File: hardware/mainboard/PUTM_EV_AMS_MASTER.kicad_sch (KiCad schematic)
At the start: 21 parts, among them J1 Conn_02x10_Odd_Even, J10 M300-MV10345M1, J3 Conn_02x04_Odd_Even, J4 FTSH-107-01-L-D-K, J5 M80-51004XX, J7 M300-MV10345M1, J8 M80-51004XX, T1 SM91502ALE

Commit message: First board revision
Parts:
- added H1: MountingHole_Pad, MountingHole:MountingHole_3.2mm_M3_Pad_Via, symbol Mechanical:MountingHole_Pad
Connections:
- net GND: now also H1.1
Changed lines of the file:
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@@
 	(wire
 		(pts
-			(xy 182.88 231.14) (xy 158.75 231.14)
+			(xy 158.75 231.14) (xy 184.15 231.14)
 		)
 		(stroke
@@
 	(wire
 		(pts
-			(xy 182.88 266.7) (xy 151.13 266.7)
+			(xy 151.13 266.7) (xy 184.15 266.7)
+		)
+		(stroke
+			(width 0)
+			(type default)
+		)
+	)
+	(wire
+		(pts
+			(xy 323.85 222.25) (xy 323.85 223.52)
 		)
 		(stroke
@@
 	(wire
 		(pts
-			(xy 182.88 264.16) (xy 153.67 264.16)
+			(xy 153.67 264.16) (xy 184.15 264.16)
 		)
 		(stroke
@@
 	(wire
 		(pts
-			(xy 182.88 261.62) (xy 156.21 261.62)
+			(xy 156.21 261.62) (xy 184.15 261.62)
 		)
 		(stroke
@@
 		(lib_name "GND_5")
 		(lib_id "power:GND")
+		(at 323.85 223.52 0)
+		(unit 1)
+		(exclude_from_sim no)
+		(in_bom yes)
+		(on_board yes)
+		(dnp no)
+		(property "Reference" "#PWR04"
+			(at 323.85 229.87 0)
+			(effects
+				(font
+					(size 1.27 1.27)
+				)
+				(hide yes)
+			)
+		)
+		(property "Value" "GND"
+			(at 323.85 227.33 0)
+			(effects
+				(font
+					(size 1.27 1.27)
+				)
+			)
+		)
+		(property "Footprint" ""
+			(at 323.85 223.52 0)
+			(effects
+				(font
+					(size 1.27 1.27)
+				)
+				(hide yes)
+			)
+		)
+		(property "Datasheet" ""
+			(at 323.85 223.52 0)
+			(effects
+				(font
+					(size 1.27 1.27)
+				)
+				(hide yes)
+			)
+		)
+		(property "Description" ""
+			(at 323.85 223.52 0)
+			(effects
+				(font
+					(size 1.27 1.27)
+				)
+				(hide yes)
+			)
+		)
+		(pin "1"
+		)
+		(instances
+			(project "PUTM_EV_AMS_MASTER"
+				(path "/b456cffc-d9d7-4c91-91f2-36ec9a65dd1b"
+					(reference "#PWR04")
+					(unit 1)
+				)
+			)
+		)
+	)
+	(symbol
+		(lib_name "GND_5")
+		(lib_id "power:GND")
 		(at 364.49 223.52 0)
 		(unit 1)
@@
 					(unit 1)
 				)
+			)
+		)
+	)
+	(symbol
+		(lib_id "Mechanical:MountingHole_Pad")
+		(at 323.85 219.71 0)
+		(unit 1)
+		(exclude_from_sim no)
+		(in_bom no)
+		(on_board yes)
+		(dnp no)
+		(fields_autoplaced yes)
+		(property "Reference" "H1"
+			(at 326.39 217.1699 0)
+			(effects
+				(font
+					(size 1.27 1.27)
+				)
+				(justify left)
+			)
+		)
+		(property "Value" "MountingHole_Pad"
+			(at 326.39 219.7099 0)
+			(effects
+				(font
+					(size 1.27 1.27)
+				)
+				(justify left)
+			)
+		)
+		(property "Footprint" "MountingHole:MountingHole_3.2mm_M3_Pad_Via"
+			(at 323.85 219.71 0)
+			(effects
+				(font
+					(size 1.27 1.27)
+				)
+				(hide yes)
+			)
+		)
+		(property "Datasheet" "~"
+			(at 323.85 219.71 0)
+			(effects
+				(font
+					(size 1.27 1.27)
+				)
+				(hide yes)
+			)
+		)
+		(property "Description" "Mounting Hole with connection"
+			(at 323.85 219.71 0)
+			(effects
+				(font
+					(size 1.27 1.27)
+				)
+				(hide yes)
+			)
+		)
+		(pin "1"
+		)
+		(instances
+			(project ""
+				(path "/b456cffc-d9d7-4c91-91f2-36ec9a65dd1b"
+					(reference "H1")
+					(unit 1)
+				)

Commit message: Layout again
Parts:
- removed H1: MountingHole_Pad, MountingHole:MountingHole_3.2mm_M3_Pad_Via, symbol Mechanical:MountingHole_Pad
- added D24, D28: 3.6V/400W, Package_TO_SOT_SMD:SOT-23-6, symbol Power_Protection:ESDA5V3SC5
- added TP19, TP20, TP21, TP22, TP23, TP24, TP25, TP26, TP27, TP28, TP29, TP30, TP31, TP32, TP33, TP34, TP35, TP36, TP37, TP38, TP39, TP40, TP41, TP42, TP43, TP44, TP45: TestPoint_Small, TestPoint:TestPoint_Pad_D1.0mm, symbol Connector:TestPoint_Small
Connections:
- net ADC/ACU_V+: now also TP38.1
- net ADC/ACU_V-: now also TP37.1
- net ADC/CAR_V+: now also TP39.1
- net ADC/CAR_V-: now also TP40.1
- net AED: now also TP26.1
- net AIR_M-: now also D28.4 (A)
- net AIR_P-: now also D28.3 (A)
- net AIR_PRE-: now also D28.1 (A)
- net AMD: now also TP27.1
- net APD: now also TP28.1
- net CAR_I: now also TP36.1
- net CRX1: now also TP22.1
- net CRX2: now also TP20.1
- net CTSMS: now also TP30.1
- net CTX1: now also TP21.1
- net CTX2: now also TP19.1
- net Connectivity/UART_RST: now also TP23.1
- net DCH: now also TP29.1
- net FAN1-: now also D24.6 (A)
- net FAN2-: now also D24.4 (A)
- net FAN3-: now also D24.3 (A)
- net FAN4-: now also D24.1 (A)
- net GND: now also D24.2 (K), D24.5 (NC), D28.2 (K), D28.5 (NC)
- net Isolated SPI/OUT+: now also TP41.1
- net Isolated SPI/OUT-: now also TP42.1
- net NRST: now also TP33.1
- net SWCLK: now also TP34.1
- net SWDIO: now also TP35.1
- net UART_DBG_RX: now also TP31.1
- net UART_DBG_TX: now also TP32.1
- net UCRX: now also TP44.1
- net UCTX: now also TP43.1
- net URX: now also TP24.1
- net UTX: now also TP25.1
- net ~{FLT}: now also TP45.1
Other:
- moved on the sheet: J3

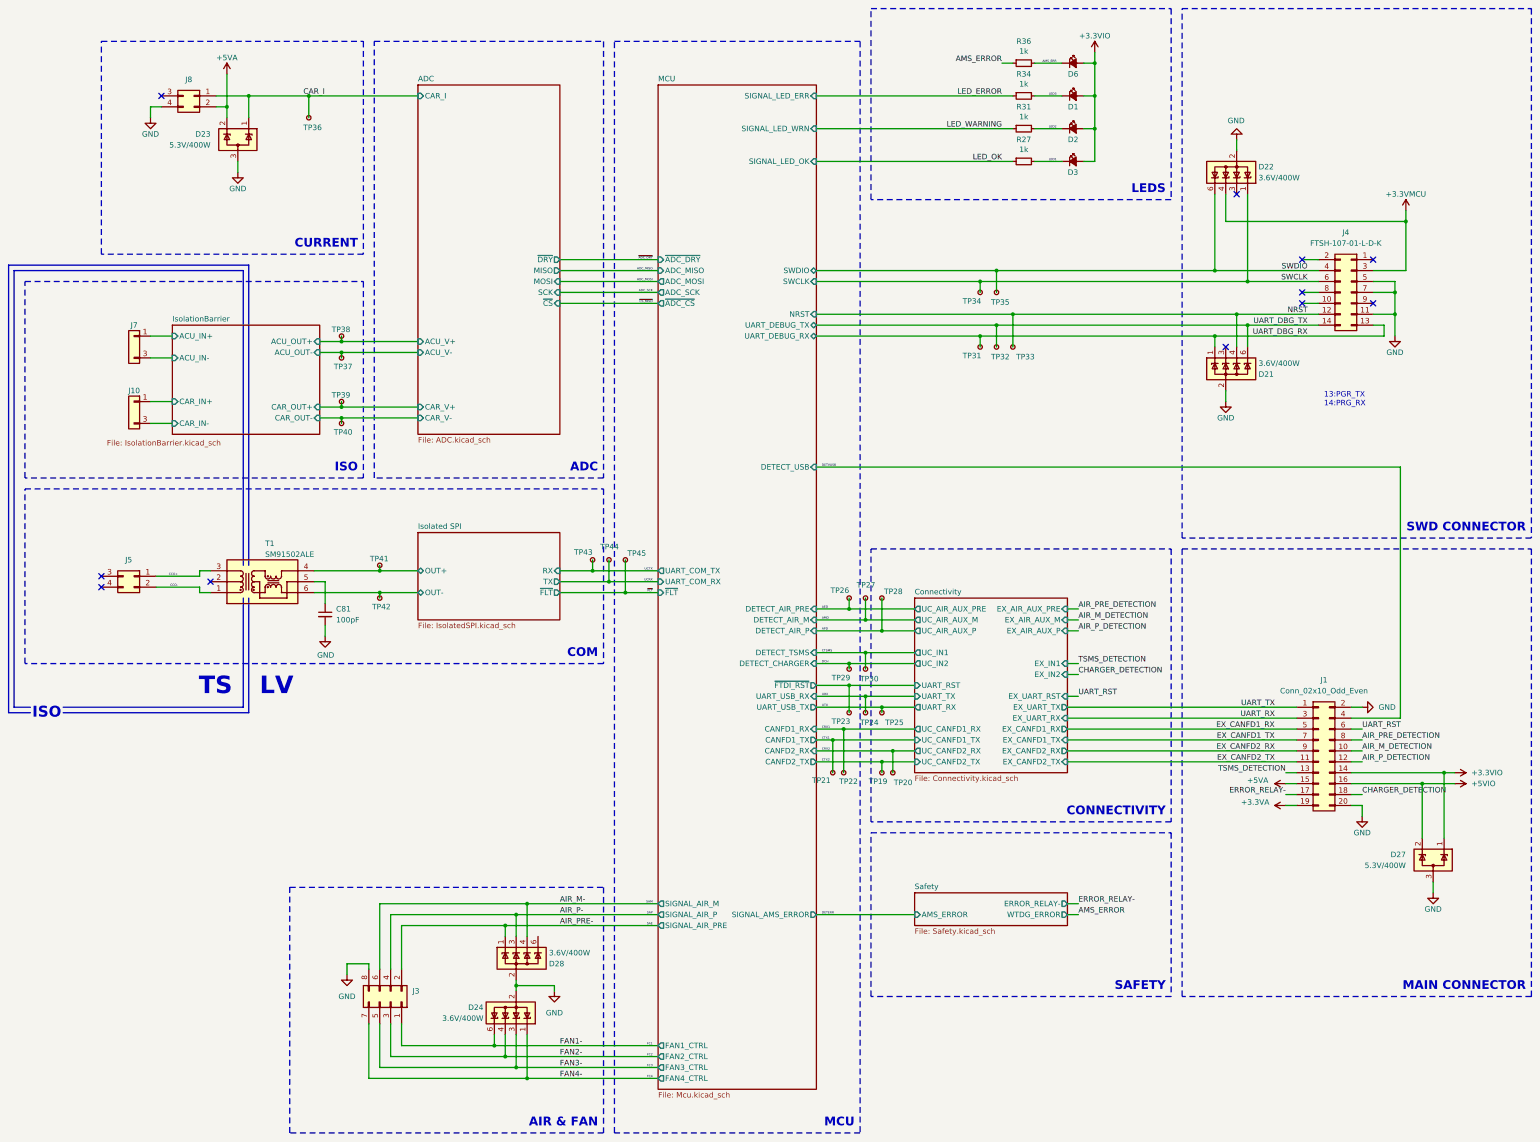
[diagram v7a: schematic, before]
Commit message: Plytka chyba fajnie zrobiona oprocz teardropow bo kicad 10 jest dziwny
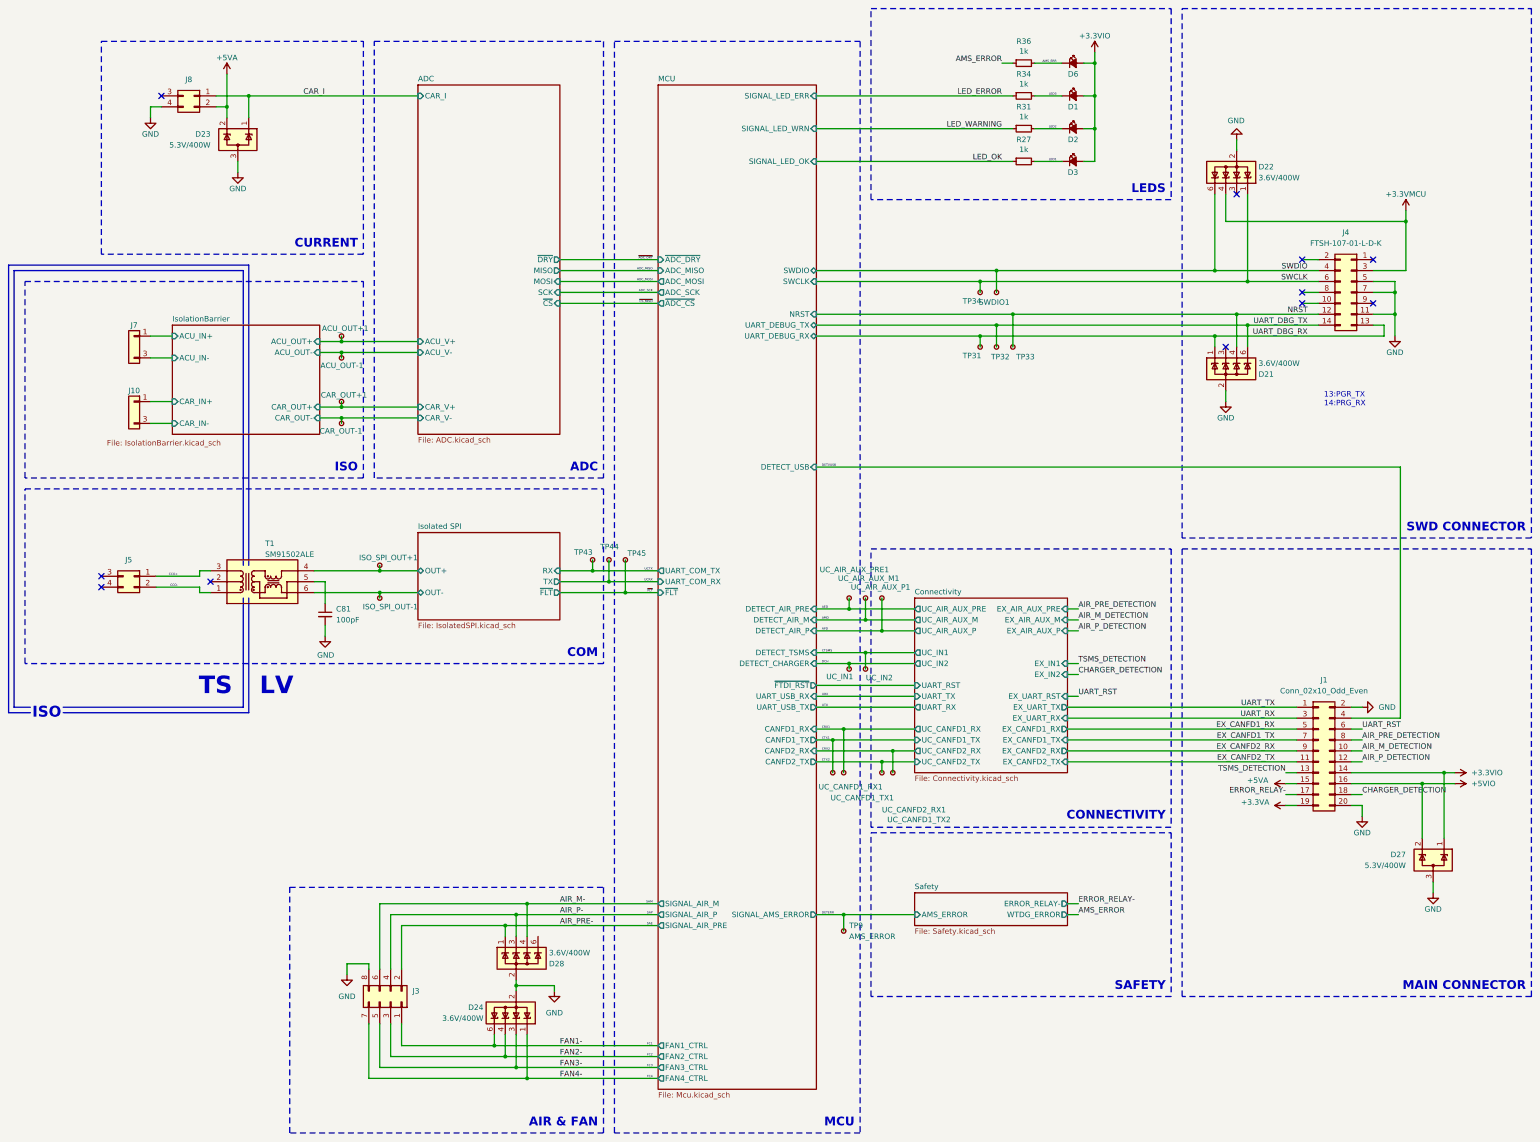
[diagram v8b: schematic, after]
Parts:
- removed TP23, TP24, TP25, TP36: TestPoint_Small, TestPoint:TestPoint_Pad_D1.0mm, symbol Connector:TestPoint_Small
- added TP9: AMS_ERROR, symbol Connector:TestPoint_Small
- ACU_OUT+1: renamed from TP38; value TestPoint_Small -> ACU_OUT+
- ACU_OUT-1: renamed from TP37; value TestPoint_Small -> ACU_OUT-
- CAR_OUT+1: renamed from TP39; value TestPoint_Small -> CAR_OUT+
- CAR_OUT-1: renamed from TP40; value TestPoint_Small -> CAR_OUT-
- ISO_SPI_OUT+1: renamed from TP41; value TestPoint_Small -> ISO_SPI_OUT+
- ISO_SPI_OUT-1: renamed from TP42; value TestPoint_Small -> ISO_SPI_OUT-
- SWDIO1: renamed from TP35; value TestPoint_Small -> SWDIO
- TP31: value TestPoint_Small -> DBG_RX
- TP32: value TestPoint_Small -> DBG_TX
- TP33: value TestPoint_Small -> NRST
- TP34: value TestPoint_Small -> SWCLK
- TP43: value TestPoint_Small -> SPI_TX
- TP44: value TestPoint_Small -> SPI_RX
- TP45: value TestPoint_Small -> FLT
- renumbered TP27 to UC_AIR_AUX_M1, TP28 to UC_AIR_AUX_P1, TP26 to UC_AIR_AUX_PRE1, TP21 to UC_CANFD1_RX1, TP22 to UC_CANFD1_TX1, TP20 to UC_CANFD1_TX2, TP19 to UC_CANFD2_RX1, TP29 to UC_IN1, TP30 to UC_IN2
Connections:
- net DETERR: now also TP9.1
